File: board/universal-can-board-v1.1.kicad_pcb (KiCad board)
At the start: 2 copper layers, 49.3 x 59.4 mm, 71 parts, among them IC1 ATMEGA328P-A, P1 USB_OTG, P2 CONN_01X08, P3 CONN_01X02, P4 CONN_01X08, P5 CONN_01X08, U1 FT232RL, U2 LM1117-3.3, U3 MCP2515-I/ST, U4 MCP2551-I/SN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

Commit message: ...
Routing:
- net VCC: track 176.2 -> 187.0 mm, vias 5 -> 6
- net GND: track 192.2 -> 197.6 mm, vias 14 -> 15
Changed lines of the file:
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@@
-(kicad_pcb (version 4) (host pcbnew 4.0.7+dfsg1-1~bpo9+1)
+(kicad_pcb (version 4) (host pcbnew 4.0.5+dfsg1-4)
   (general
     (links 173)
-    (no_connects 13)
+    (no_connects 12)
     (area 120.828999 50.724999 170.255001 110.311001)
     (thickness 1.6)
     (drawings 7)
-    (tracks 594)
+    (tracks 606)
     (zones 0)
     (modules 71)
@@
   (segment (start 153.924 98.044) (end 153.924 97.044) (width 0.4) (layer B.Cu) (net 1))
   (segment (start 154.555 98.675) (end 153.924 98.044) (width 0.4) (layer B.Cu) (net 1))
-  (segment (start 157.988 103.616) (end 155.44 103.616) (width 0.4) (layer F.Cu) (net 2) (status C00000))
-  (segment (start 155.44 103.616) (end 154.94 104.116) (width 0.4) (layer F.Cu) (net 2) (status C00000))
-  (segment (start 161.234 98.984) (end 161.234 96.234) (width 0.4) (layer F.Cu) (net 2) (status C00000))
-  (segment (start 161.234 96.234) (end 161.334 96.134) (width 0.4) (layer F.Cu) (net 2) (status C00000))
-  (segment (start 148.8 101.925) (end 151.059 101.925) (width 0.4) (layer B.Cu) (net 2) (status 400000))
-  (segment (start 153.659 99.325) (end 156 99.325) (width 0.4) (layer B.Cu) (net 2) (status 800000))
+  (segment (start 156 99.325) (end 157.723 99.325) (width 0.4) (layer B.Cu) (net 2) (status 400000))
+  (segment (start 158.064 98.984) (end 161.234 98.984) (width 0.4) (layer F.Cu) (net 2) (status 800000))
+  (segment (start 157.988 99.06) (end 158.064 98.984) (width 0.4) (layer F.Cu) (net 2))
+  (via (at 157.988 99.06) (size 0.6) (drill 0.4) (layers F.Cu B.Cu) (net 2))
+  (segment (start 157.723 99.325) (end 157.988 99.06) (width 0.4) (layer B.Cu) (net 2))
+  (segment (start 157.988 103.616) (end 155.44 103.616) (width 0.4) (layer F.Cu) (net 2))
+  (segment (start 155.44 103.616) (end 154.94 104.116) (width 0.4) (layer F.Cu) (net 2))
+  (segment (start 161.234 98.984) (end 161.234 96.234) (width 0.4) (layer F.Cu) (net 2))
+  (segment (start 161.234 96.234) (end 161.334 96.134) (width 0.4) (layer F.Cu) (net 2))
+  (segment (start 148.8 101.925) (end 151.059 101.925) (width 0.4) (layer B.Cu) (net 2))
+  (segment (start 153.659 99.325) (end 156 99.325) (width 0.4) (layer B.Cu) (net 2))
   (segment (start 151.059 101.925) (end 153.659 99.325) (width 0.4) (layer B.Cu) (net 2))
-  (segment (start 156 101.275) (end 153.741 101.275) (width 0.4) (layer B.Cu) (net 2) (status 400000))
+  (segment (start 156 101.275) (end 153.741 101.275) (width 0.4) (layer B.Cu) (net 2))
   (segment (start 152.892 102.124) (end 152.892 105.172) (width 0.4) (layer B.Cu) (net 2))
   (segment (start 153.741 101.275) (end 152.892 102.124) (width 0.4) (layer B.Cu) (net 2))
-  (segment (start 156 103.875) (end 156 104.525) (width 0.4) (layer B.Cu) (net 2) (status C00000))
-  (segment (start 152.892 108.204) (end 152.892 105.172) (width 0.4) (layer B.Cu) (net 2) (status 400000))
-  (segment (start 153.539 104.525) (end 156 104.525) (width 0.4) (layer B.Cu) (net 2) (status 800000))
+  (segment (start 156 103.875) (end 156 104.525) (width 0.4) (layer B.Cu) (net 2))
+  (segment (start 152.892 108.204) (end 152.892 105.172) (width 0.4) (layer B.Cu) (net 2))
+  (segment (start 153.539 104.525) (end 156 104.525) (width 0.4) (layer B.Cu) (net 2))
   (segment (start 152.892 105.172) (end 153.539 104.525) (width 0.4) (layer B.Cu) (net 2))
-  (segment (start 141.546 88.792) (end 139.808 88.792) (width 0.4) (layer F.Cu) (net 2) (status 400000))
+  (segment (start 141.546 88.792) (end 139.808 88.792) (width 0.4) (layer F.Cu) (net 2))
   (segment (start 139.808 88.792) (end 139.7 88.9) (width 0.4) (layer F.Cu) (net 2))
-  (segment (start 138.176 88.884) (end 139.684 88.884) (width 0.4) (layer F.Cu) (net 2) (status 400000))
+  (segment (start 138.176 88.884) (end 139.684 88.884) (width 0.4) (layer F.Cu) (net 2))
   (segment (start 139.684 88.884) (end 139.7 88.9) (width 0.4) (layer F.Cu) (net 2))
   (via (at 138.684 95.504) (size 0.6) (drill 0.4) (layers F.Cu B.Cu) (net 2))
@@
   (segment (start 153.416 56.642) (end 157.226 56.642) (width 0.6) (layer F.Cu) (net 2))
   (segment (start 166.624 95.924) (end 166.834 96.134) (width 0.8) (layer F.Cu) (net 2))
-  (segment (start 150.892 108.204) (end 150.892 107.68) (width 0.4) (layer B.Cu) (net 3) (status C00000))
-  (segment (start 150.892 107.68) (end 151.892 106.68) (width 0.4) (layer B.Cu) (net 3) (status 400000))
+  (segment (start 148.352 78.232) (end 148.352 80.28) (width 0.4) (layer F.Cu) (net 3) (status 400000))
+  (segment (start 152.4 84.328) (end 152.4 87.376) (width 0.4) (layer B.Cu) (net 3))
+  (segment (start 150.876 82.804) (end 152.4 84.328) (width 0.4) (layer B.Cu) (net 3))
+  (via (at 150.876 82.804) (size 0.6) (drill 0.4) (layers F.Cu B.Cu) (net 3))
+  (segment (start 148.352 80.28) (end 150.876 82.804) (width 0.4) (layer F.Cu) (net 3))
+  (segment (start 150.892 108.204) (end 150.892 107.68) (width 0.4) (layer B.Cu) (net 3))
+  (segment (start 150.892 107.68) (end 151.892 106.68) (width 0.4) (layer B.Cu) (net 3))
   (segment (start 153.375 100.625) (end 151.892 102.108) (width 0.4) (layer B.Cu) (net 3))
   (segment (start 151.892 102.108) (end 151.892 103.632) (width 0.4) (layer B.Cu) (net 3))
-  (segment (start 156 100.625) (end 153.375 100.625) (width 0.4) (layer B.Cu) (net 3) (status 400000))
+  (segment (start 156 100.625) (end 153.375 100.625) (width 0.4) (layer B.Cu) (net 3))
   (segment (start 151.892 106.68) (end 151.892 103.632) (width 0.4) (layer B.Cu) (net 3))
   (segment (start 135.128 52.848) (end 135.128 52.832) (width 0.4) (layer B.Cu) (net 3))
@@
   (via (at 148.844 58.42) (size 0.6) (drill 0.4) (layers F.Cu B.Cu) (net 48))
   (segment (start 149.225 58.039) (end 148.844 58.42) (width 0.4) (layer B.Cu) (net 48))
-  (segment (start 156 97.375) (end 158.843 97.375) (width 0.4) (layer B.Cu) (net 59))
-  (segment (start 163.576 100.584) (end 161.234 100.584) (width 0.4) (layer F.Cu) (net 59))
+  (segment (start 158.843 97.375) (end 159.351 97.375) (width 0.4) (layer B.Cu) (net 59))
+  (segment (start 160.528 100.584) (end 163.576 100.584) (width 0.4) (layer B.Cu) (net 59))
   (via (at 163.576 100.584) (size 0.6) (drill 0.4) (layers F.Cu B.Cu) (net 59))
-  (segment (start 160.02 100.584) (end 163.576 100.584) (width 0.4) (layer B.Cu) (net 59))
-  (segment (start 159.512 100.076) (end 160.02 100.584) (width 0.4) (layer B.Cu) (net 59))
-  (segment (start 159.512 98.044) (end 159.512 100.076) (width 0.4) (layer B.Cu) (net 59))
-  (segment (start 158.843 97.375) (end 159.512 98.044) (width 0.4) (layer B.Cu) (net 59))
-  (segment (start 156 98.025) (end 157.969 98.025) (width 0.4) (layer B.Cu) (net 60))
-  (segment (start 163.36 101.384) (end 161.234 101.384) (width 0.4) (layer F.Cu) (net 60))
-  (segment (start 163.576 101.6) (end 163.36 101.384) (width 0.4) (layer F.Cu) (net 60))
+  (segment (start 161.234 100.584) (end 163.576 100.584) (width 0.4) (layer F.Cu) (net 59))
+  (segment (start 158.843 97.375) (end 156 97.375) (width 0.4) (layer B.Cu) (net 59))
+  (segment (start 160.02 100.076) (end 160.528 100.584) (width 0.4) (layer B.Cu) (net 59))
+  (segment (start 160.02 98.044) (end 160.02 100.076) (width 0.4) (layer B.Cu) (net 59))
+  (segment (start 159.351 97.375) (end 160.02 98.044) (width 0.4) (layer B.Cu) (net 59))
+  (segment (start 157.969 98.025) (end 158.477 98.025) (width 0.4) (layer B.Cu) (net 60))
+  (segment (start 160.02 101.6) (end 163.576 101.6) (width 0.4) (layer B.Cu) (net 60))
   (via (at 163.576 101.6) (size 0.6) (drill 0.4) (layers F.Cu B.Cu) (net 60))
-  (segment (start 159.512 101.6) (end 163.576 101.6) (width 0.4) (layer B.Cu) (net 60))
-  (segment (start 158.496 100.584) (end 159.512 101.6) (width 0.4) (layer B.Cu) (net 60))
-  (segment (start 158.496 98.552) (end 158.496 100.584) (width 0.4) (layer B.Cu) (net 60))
-  (segment (start 157.969 98.025) (end 158.496 98.552) (width 0.4) (layer B.Cu) (net 60))
+  (segment (start 163.576 101.6) (end 163.36 101.384) (width 0.4) (layer F.Cu) (net 60))
+  (segment (start 161.234 101.384) (end 163.36 101.384) (width 0.4) (layer F.Cu) (net 60))
+  (segment (start 157.969 98.025) (end 156 98.025) (width 0.4) (layer B.Cu) (net 60))
+  (segment (start 159.004 100.584) (end 160.02 101.6) (width 0.4) (layer B.Cu) (net 60))
+  (segment (start 159.004 98.552) (end 159.004 100.584) (width 0.4) (layer B.Cu) (net 60))
+  (segment (start 158.477 98.025) (end 159.004 98.552) (width 0.4) (layer B.Cu) (net 60))
   (segment (start 149.225 61.12) (end 149.225 61.595) (width 0.4) (layer B.Cu) (net 64))
   (segment (start 149.225 61.595) (end 147.828 62.992) (width 0.4) (layer B.Cu) (net 64))

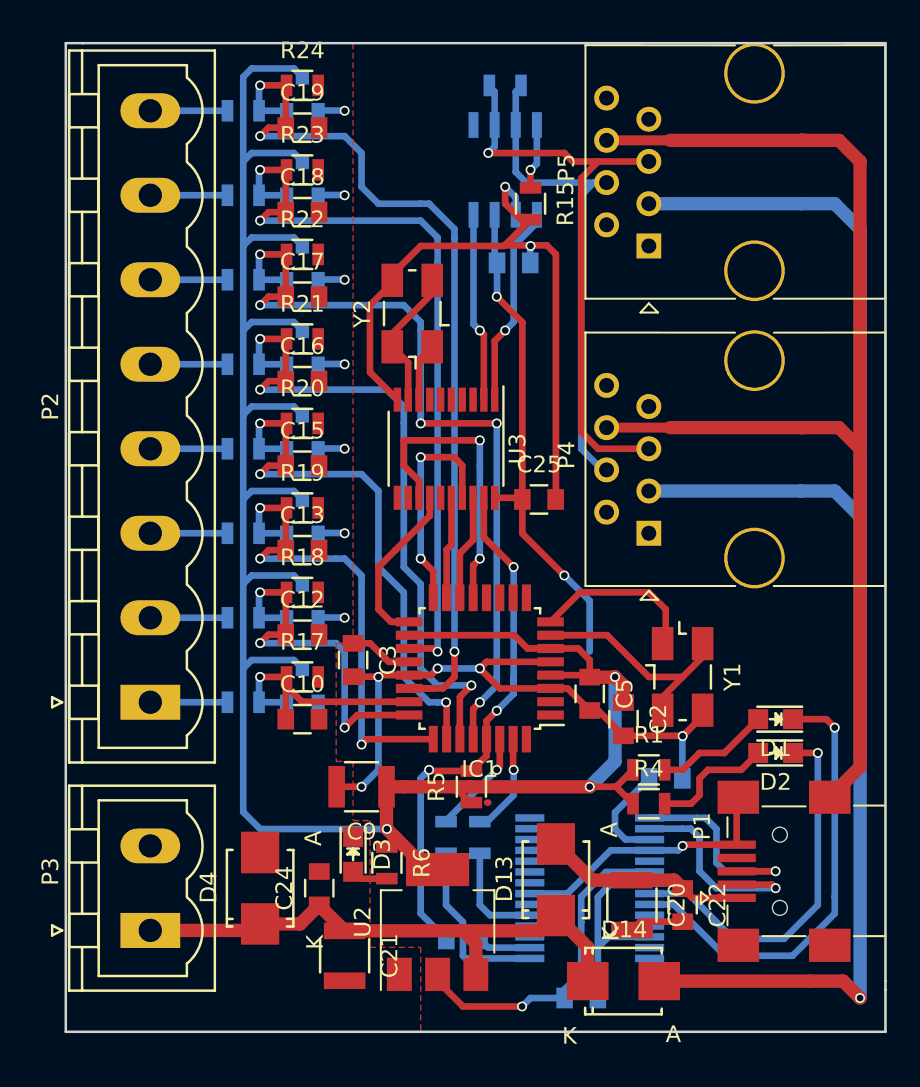
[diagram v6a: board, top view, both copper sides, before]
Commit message: Added last missing parts and changed some routings.
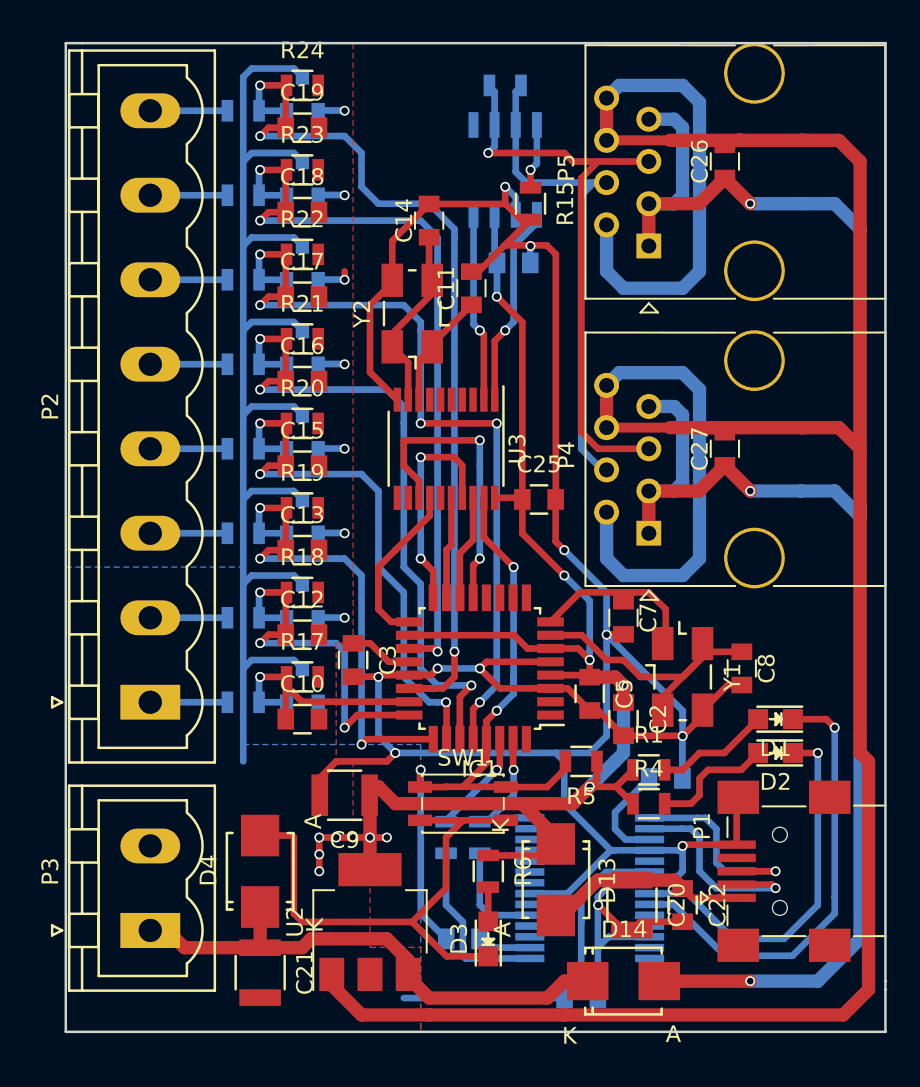
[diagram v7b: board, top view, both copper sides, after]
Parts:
- removed C24: 100n, Capacitors_SMD:C_0805
- added C11: 11p, Capacitors_SMD:C_0805, F.Cu at (145.3, 65.5)
- added C14: 11p, Capacitors_SMD:C_0805, F.Cu at (142.7, 61.5)
- added C26: 100n, Capacitors_SMD:C_0805, F.Cu at (160.5, 57.9)
- added C27: 100n, Capacitors_SMD:C_0805, F.Cu at (160.5, 75.2)
- added C7: 11p, Capacitors_SMD:C_0805, F.Cu at (154.4, 85.3)
- added C8: 11p, Capacitors_SMD:C_0805, F.Cu at (161.5, 88.4)
- added SW1: SW_Push, Buttons_Switches_SMD:SW_SPST_EVQP2, F.Cu at (144.8, 96.5)
- moved D3 9.58 mm to (146.3, 104.6), turned to 90 degrees
- moved R5 6.78 mm to (151.9, 94.0), turned to 180 degrees
- moved R6 6.12 mm to (146.3, 100.6)
- moved C21 5.18 mm to (132.6, 106.7)
- moved U2 4.06 mm to (139.2, 103.6)
- moved C9 1.14 mm to (137.7, 96.0)
- moved D4 1.02 mm to (132.6, 100.6)
- turned D13 to 270 degrees
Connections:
- D13 pad 1: +5V -> VCC
- D14 pad 2: Net-(D14-Pad2) -> Net-(C26-Pad1)
- P4 pad 1: Net-(P4-Pad1) -> Net-(C26-Pad1)
- P4 pad 2: Net-(P4-Pad2) -> GND
- P4 pad 3: Net-(D14-Pad2) -> Net-(C26-Pad1)
- P4 pad 7: Net-(P4-Pad7) -> Net-(C26-Pad1)
- P4 pad 8: Net-(P4-Pad8) -> GND
- P5 pad 1: Net-(P5-Pad1) -> Net-(C26-Pad1)
- P5 pad 2: Net-(P5-Pad2) -> GND
- P5 pad 3: Net-(D14-Pad2) -> Net-(C26-Pad1)
- P5 pad 7: Net-(P5-Pad7) -> Net-(C26-Pad1)
- P5 pad 8: Net-(P5-Pad8) -> GND
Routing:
- net GND: track 197.6 -> 400.0 mm, vias 15 -> 18
- net Net-(C26-Pad1): track 0.00 -> 107.2 mm, vias 0 -> 3
- net Net-(D14-Pad2): track 85.4 -> 0.00 mm, vias 1 -> 0
- net RESET: track 33.3 -> 42.1 mm
- net VCC: track 187.0 -> 194.4 mm, vias 6 -> 12
- net Net-(C8-Pad1): track 14.0 -> 18.2 mm
- net Net-(C11-Pad1): track 3.51 -> 7.01 mm
- net Net-(C14-Pad1): track 8.57 -> 11.2 mm
- net +5V: track 33.8 -> 31.9 mm
- net Net-(C7-Pad1): track 10.2 -> 11.0 mm
- added copper zone on B.Cu, net VCC
